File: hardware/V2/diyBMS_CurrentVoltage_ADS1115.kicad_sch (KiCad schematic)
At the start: 53 parts, among them J3 Debug/UPDI, J3 PA3/PA4, J4 9x9 PIN connector, J5 9x9 PIN connector, J5 Screw_Terminal_01x04, J6 Screw_Terminal_01x02, J7 Screw_Terminal_01x02, U1 ACPL-C870, U2 ADS1115IDGS, U2 ATtiny1614-SS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

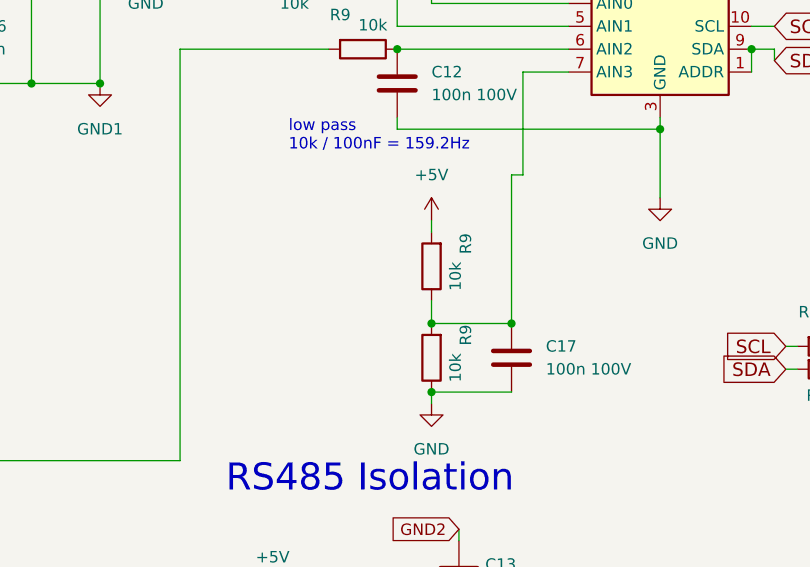
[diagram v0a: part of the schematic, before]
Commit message: Added hardware V1, added trimmer to hardware V2, fixed parity between schematic & gerber
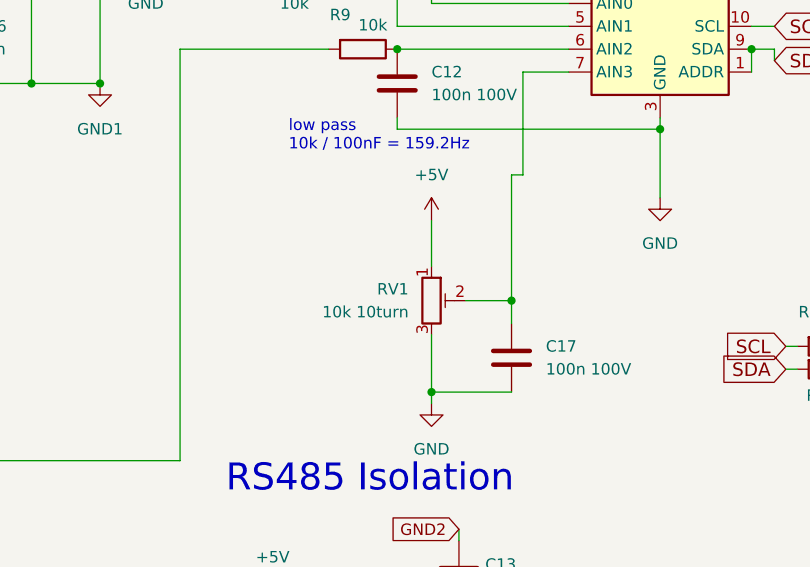
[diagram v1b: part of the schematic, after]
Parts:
- removed R9 (x2): 10k, Resistor_SMD:R_0805_2012Metric, symbol Device:R
- added RV1: 10k 10turn, Potentiometer_THT:Potentiometer_Bourns_3299W_Vertical, symbol Device:R_Potentiometer_Trim
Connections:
- net +5V: now also RV1.1
- net GND: now also RV1.3
- net at C17.1, U2.7 (AIN3): now also RV1.2
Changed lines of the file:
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@@
   (junction (at 152.4 87.63) (diameter 0) (color 0 0 0 0)
   )
+  (junction (at 127 116.84) (diameter 0) (color 0 0 0 0)
+  )
   (junction (at 162.56 78.74) (diameter 0) (color 0 0 0 0)
   )
@@
   (junction (at 147.32 39.37) (diameter 0) (color 0 0 0 0)
   )
-  (junction (at 135.89 109.22) (diameter 0) (color 0 0 0 0)
-  )
   (junction (at 156.21 31.75) (diameter 0) (color 0 0 0 0)
   )
   (junction (at 238.76 37.465) (diameter 0) (color 0 0 0 0)
   )
+  (junction (at 135.89 106.68) (diameter 0) (color 0 0 0 0)
+  )
   (junction (at 46.99 82.55) (diameter 0) (color 0 0 0 0)
   )
@@
   (junction (at 139.954 169.926) (diameter 0) (color 0 0 0 0)
   )
-  (junction (at 127 116.84) (diameter 0) (color 0 0 0 0)
-  )
   (junction (at 90.17 31.75) (diameter 0) (color 0 0 0 0)
   )
@@
   )
   (junction (at 137.16 31.75) (diameter 0) (color 0 0 0 0)
-  )
-  (junction (at 127 109.22) (diameter 0) (color 0 0 0 0)
   )
   (junction (at 105.41 39.37) (diameter 0) (color 0 0 0 0)
@@
     (stroke (width 0) (type default))
   )
+  (wire (pts (xy 135.89 106.68) (xy 135.89 92.71))
+    (stroke (width 0) (type default))
+  )
   (wire (pts (xy 106.68 55.88) (xy 102.87 55.88))
     (stroke (width 0) (type default))
@@
     (stroke (width 0) (type default))
   )
-  (wire (pts (xy 135.89 109.22) (xy 135.89 92.71))
+  (wire (pts (xy 135.89 109.22) (xy 135.89 106.68))
     (stroke (width 0) (type default))
   )
@@
     (stroke (width 0) (type default))
   )
-  (wire (pts (xy 127 97.79) (xy 127 99.06))
+  (wire (pts (xy 127 97.79) (xy 127 102.87))
     (stroke (width 0) (type default))
   )
@@
     (stroke (width 0) (type default))
   )
-  (wire (pts (xy 127 109.22) (xy 135.89 109.22))
+  (wire (pts (xy 127 110.49) (xy 127 116.84))
     (stroke (width 0) (type default))
   )
@@
     (stroke (width 0) (type default))
   )
+  (wire (pts (xy 130.81 106.68) (xy 135.89 106.68))
+    (stroke (width 0) (type default))
+  )
   (wire (pts (xy 141.986 169.926) (xy 141.986 157.226))
     (stroke (width 0) (type default))
@@
   )
   (wire (pts (xy 123.19 58.42) (xy 124.46 58.42))
-    (stroke (width 0) (type default))
-  )
-  (wire (pts (xy 127 106.68) (xy 127 109.22))
     (stroke (width 0) (type default))
   )
@@
     )
   )
-  (symbol (lib_id "Device:R") (at 127 102.87 180) (unit 1)
-    (in_bom yes) (on_board yes) (dnp no)
-    (property "Reference" "R9" (at 130.81 99.187 90)
-      (effects (font (size 1.27 1.27)) (justify left))
-    )
-    (property "Value" "10k" (at 129.667 102.362 90)
-      (effects (font (size 1.27 1.27)) (justify left))
-    )
-    (property "Footprint" "Resistor_SMD:R_0805_2012Metric" (at 128.778 102.87 90)
-      (effects (font (size 1.27 1.27)) hide)
-    )
-    (property "Datasheet" "~" (at 127 102.87 0)
-      (effects (font (size 1.27 1.27)) hide)
-    )
-    (property "LCSCStockCode" "C17673" (at 127 102.87 0)
-      (effects (font (size 1.27 1.27)) hide)
-    )
-    (property "PartNumber" "0805W8F4701T5E" (at 127 102.87 0)
-      (effects (font (size 1.27 1.27)) hide)
-    )
-    (pin "1")
-    (pin "2")
-    (instances
-      (project "CurrentShuntCircuit"
-        (path "/2682a95a-2af7-40b5-9d59-bcba0793e9ae"
-          (reference "R9") (unit 1)
-        )
-      )
-      (project "diyBMS_CurrentVoltage_ADS1115"
-        (path "/8ce756dc-ec78-4f94-a5d4-2a0ea3f038bf"
-          (reference "R18") (unit 1)
-        )
-      )
-    )
-  )
   (symbol (lib_id "Connector:Conn_01x01_Pin") (at 34.29 121.92 0) (mirror x) (unit 1)
     (in_bom yes) (on_board yes) (dnp no)
@@
     )
   )
-  (symbol (lib_id "Device:R") (at 127 113.03 180) (unit 1)
-    (in_bom yes) (on_board yes) (dnp no)
-    (property "Reference" "R9" (at 130.81 109.347 90)
-      (effects (font (size 1.27 1.27)) (justify left))
-    )
-    (property "Value" "10k" (at 129.667 112.522 90)
-      (effects (font (size 1.27 1.27)) (justify left))
-    )
-    (property "Footprint" "Resistor_SMD:R_0805_2012Metric" (at 128.778 113.03 90)
-      (effects (font (size 1.27 1.27)) hide)
-    )
-    (property "Datasheet" "~" (at 127 113.03 0)
-      (effects (font (size 1.27 1.27)) hide)
-    )
-    (property "LCSCStockCode" "C17673" (at 127 113.03 0)
-      (effects (font (size 1.27 1.27)) hide)
-    )
-    (property "PartNumber" "0805W8F4701T5E" (at 127 113.03 0)
-      (effects (font (size 1.27 1.27)) hide)
-    )
-    (pin "1")
-    (pin "2")
-    (instances
-      (project "CurrentShuntCircuit"
-        (path "/2682a95a-2af7-40b5-9d59-bcba0793e9ae"
-          (reference "R9") (unit 1)
-        )
-      )
-      (project "diyBMS_CurrentVoltage_ADS1115"
-        (path "/8ce756dc-ec78-4f94-a5d4-2a0ea3f038bf"
-          (reference "R19") (unit 1)
-        )
-      )
-    )
-  )
   (symbol (lib_id "power:GND") (at 198.501 120.142 0) (unit 1)
     (in_bom yes) (on_board yes) (dnp no)
@@
         )
       )
+    )
+  )
+  (symbol (lib_id "Device:R_Potentiometer_Trim") (at 127 106.68 0) (unit 1)
+    (in_bom yes) (on_board yes) (dnp no) (fields_autoplaced)
+    (property "Reference" "RV1" (at 124.46 105.41 0)
+      (effects (font (size 1.27 1.27)) (justify right))
+    )
+    (property "Value" "10k 10turn" (at 124.46 107.95 0)
+      (effects (font (size 1.27 1.27)) (justify right))
+    )
+    (property "Footprint" "Potentiometer_THT:Potentiometer_Bourns_3299W_Vertical" (at 127 106.68 0)
+      (effects (font (size 1.27 1.27)) hide)
+    )
+    (property "Datasheet" "~" (at 127 106.68 0)
+      (effects (font (size 1.27 1.27)) hide)
+    )
+    (pin "2")
+    (pin "1")
+    (pin "3")
+    (instances
+      (project "diyBMS_CurrentVoltage_ADS1115"
+        (path "/8ce756dc-ec78-4f94-a5d4-2a0ea3f038bf"
+          (reference "RV1") (unit 1)
+        )
+      )
